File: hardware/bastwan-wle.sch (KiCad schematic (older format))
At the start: 29 parts, among them J1 USB_B_Micro, J2 Conn_Right, J3 Conn_Left, J4 Conn_Battery, J5 SWD, Q1 DMG3415U-7, SW1 RST, U1 RAK3172, U2 MCP1700-1202E_SOT23, U3 CP2102N-A01-GQFN28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

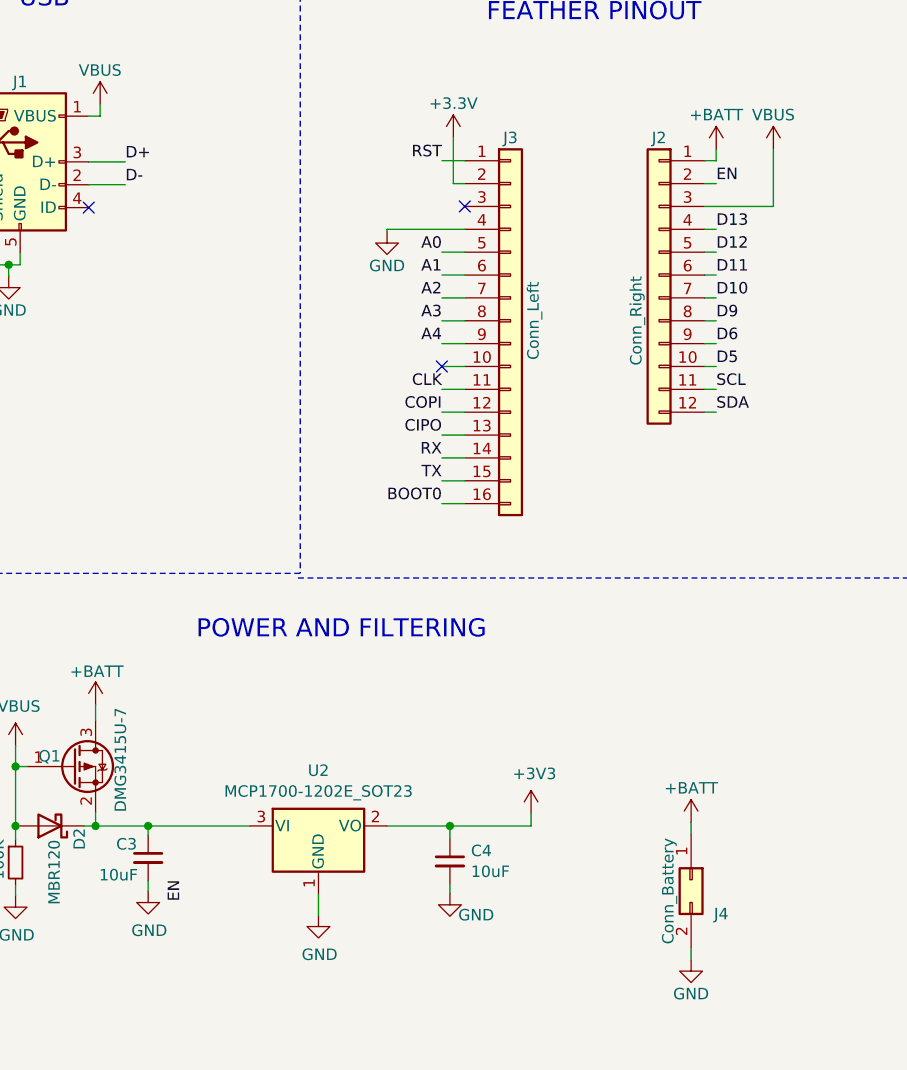
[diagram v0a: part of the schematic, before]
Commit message: remove Enable pin
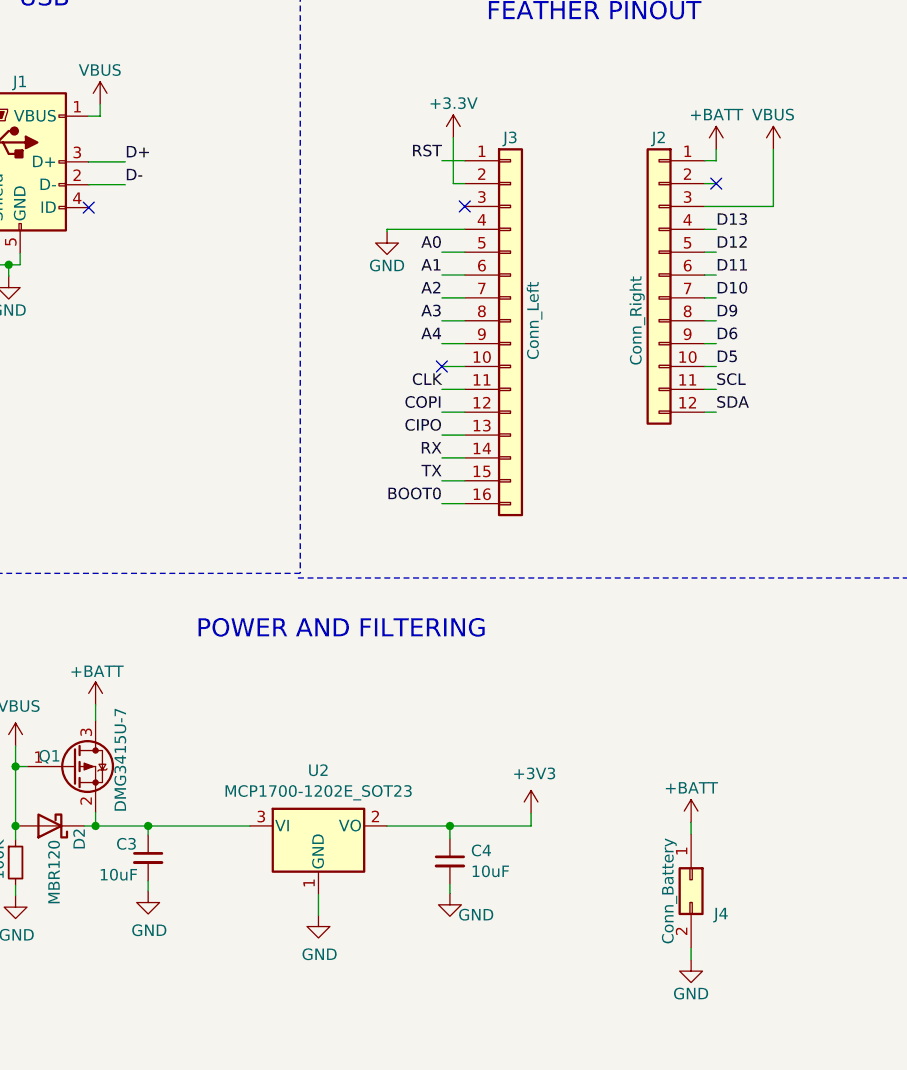
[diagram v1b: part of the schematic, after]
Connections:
- net EN: no longer names the net of J2.2 (Pin_2)
- no-connect marks 22 -> 23
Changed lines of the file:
@@
 Wire Wire Line
 	3900 1425 3950 1425
-Text Label 3950 1425 0    50   ~ 0
-EN
 $Comp
 L Connector_Generic:Conn_02x01 J4
@@
 Text Label 8145 4575 0    79   ~ 0
 D13
-Text Label 1620 4470 3    50   ~ 0
-EN
 Wire Notes Line
 	2400 5375 2400 7825
@@
 Wire Wire Line
 	1465 4235 1910 4235
+NoConn ~ 3950 1425
 $EndSCHEMATC
